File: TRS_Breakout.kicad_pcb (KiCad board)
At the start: 2 copper layers, 33.4 x 22.9 mm, 3 parts, among them J1 AudioJack3_Switch, J2 Screw_Terminal_01x06

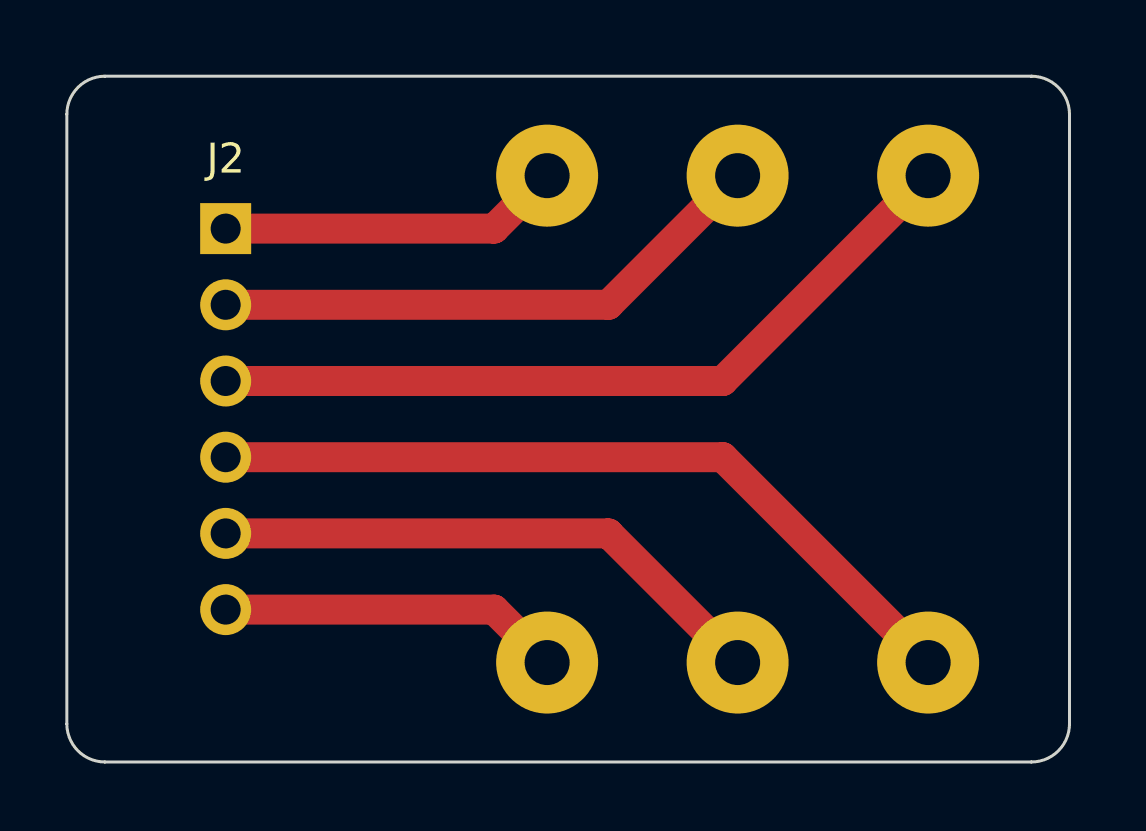
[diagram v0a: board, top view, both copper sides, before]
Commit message: Fixed solder pad art.
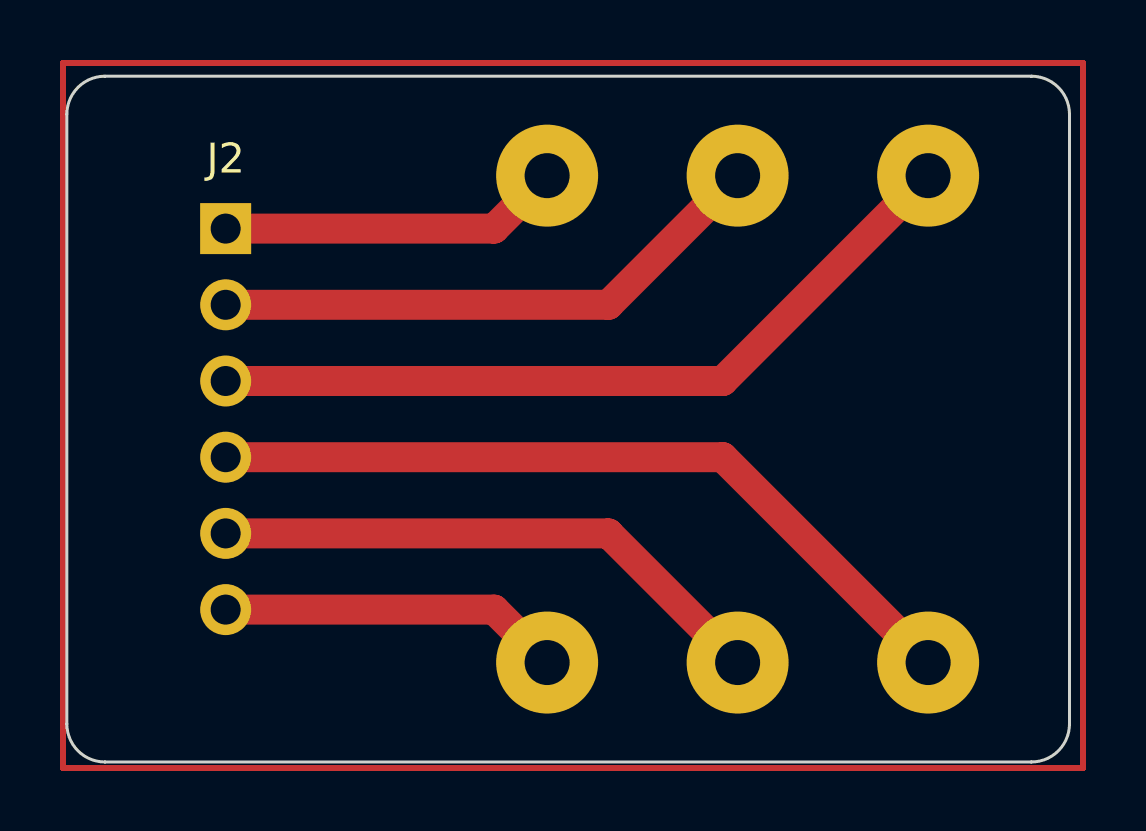
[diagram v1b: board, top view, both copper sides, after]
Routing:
- added copper zone on B.Cu, net (none)
- added copper zone on F.Cu, net (none)
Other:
- board text added: "Rng"
- board text removed: "Ring"
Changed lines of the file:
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@@
       ) (layer "B.Mask") (width 0) (fill solid))
   )
+  (gr_rect (start 112.5 91) (end 146.5 114.5) (layer "F.Cu") (width 0.2) (fill none))
   (gr_line (start 113.898026 114.3) (end 144.78 114.3) (layer "Edge.Cuts") (width 0.1))
   (gr_arc (start 113.898026 114.3) (mid 113 113.928026) (end 112.628026 113.03) (layer "Edge.Cuts") (width 0.1))
@@
     (effects (font (size 1 1) (thickness 0.15)))
   )
-  (gr_text "Tip" (at 128.6375 97.536) (layer "F.Mask")
+  (gr_text "Tip" (at 128.6375 97.41) (layer "F.Mask")
     (effects (font (size 1 1) (thickness 0.15)))
   )
-  (gr_text "Ring" (at 114.428572 99.06) (layer "F.Mask")
+  (gr_text "Rng\n" (at 114.666667 99.06) (layer "F.Mask")
     (effects (font (size 1 1) (thickness 0.15)))
   )
@@
     (effects (font (size 1 1) (thickness 0.15)))
   )
-  (gr_text "Ring" (at 134.9875 97.536) (layer "F.Mask")
+  (gr_text "Rng" (at 134.9875 97.536) (layer "F.Mask")
     (effects (font (size 1 1) (thickness 0.15)))
   )
@@
   (segment (start 126.8725 109.22) (end 128.6375 110.985) (width 1) (layer "F.Cu") (net 6))
   (segment (start 117.921875 109.22) (end 126.8725 109.22) (width 1) (layer "F.Cu") (net 6))
+  (zone (net 0) (net_name "") (layers F&B.Cu) (hatch edge 0.508)
+    (connect_pads (clearance 0.1))
+    (min_thickness 0.1) (filled_areas_thickness no)
+    (fill yes (thermal_gap 0.508) (thermal_bridge_width 0.508))
+    (polygon
+      (pts
+        (xy 112.5 91)
+        (xy 146.5 91)
+        (xy 146.5 114.5)
+        (xy 112.5 114.5)
+      )
+    )
+  )
 )
